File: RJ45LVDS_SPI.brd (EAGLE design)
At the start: 44.2 x 38 mm, 45 parts, among them J1 RJHSE-3381, U1 SN65MLVD206, U2 SN65MLVD206, U3 SN65MLVD206, U4 SN65MLVD206, U5 SN74LVC1T45DBVR, U6 SN74LVC1T45DBVR, U7 SN74LVC1T45DBVR, U8 SN74LVC1T45DBVR, U9 MIC39100-3.3WS

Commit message: tweaks
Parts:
- removed SJ13: (no value), jumper:SJ
- moved R5 6.60 mm to (36.5, 74.2)
- moved C14 0.23 mm to (14.5, 42.9)
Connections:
- removed net N$18: R5.2, SJ13.2
- net +3V3: now also R5.2; no longer SJ13.1
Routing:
- net N$18: track 4.46 -> 0.00 mm, vias 1 -> 0
- net N$19: track 4.63 -> 7.30 mm
- net N$15: track 41.1 -> 39.8 mm
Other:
- board text removed: "LED_EN"

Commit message: Bom added
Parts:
- added C11: .1u, rcl-dhs:C0603
- C10, C16, C9: device rcl-dhs:C1206K -> rcl:SMC_B
- moved R5 5.19 mm to (39.9, 70.3), turned to 90 degrees
- moved U9 0.74 mm to (44.4, 64.5)
- moved C16 0.56 mm to (46.5, 58.7)
- moved C10 0.35 mm to (43.6, 69.8)
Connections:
- net +3V3: now also C9.+; no longer C9.1
- net +5V: now also C10.+, C11.1; no longer C10.1
- net GND: now also C10.-, C11.2, C16.-, C9.-; no longer C10.2, C16.2, C9.2
- net N$16: now also C16.+; no longer C16.1
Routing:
- net N$19: track 7.30 -> 12.0 mm
- net N$17: track 3.72 -> 2.98 mm
- net +5V: track 6.54 -> 7.25 mm

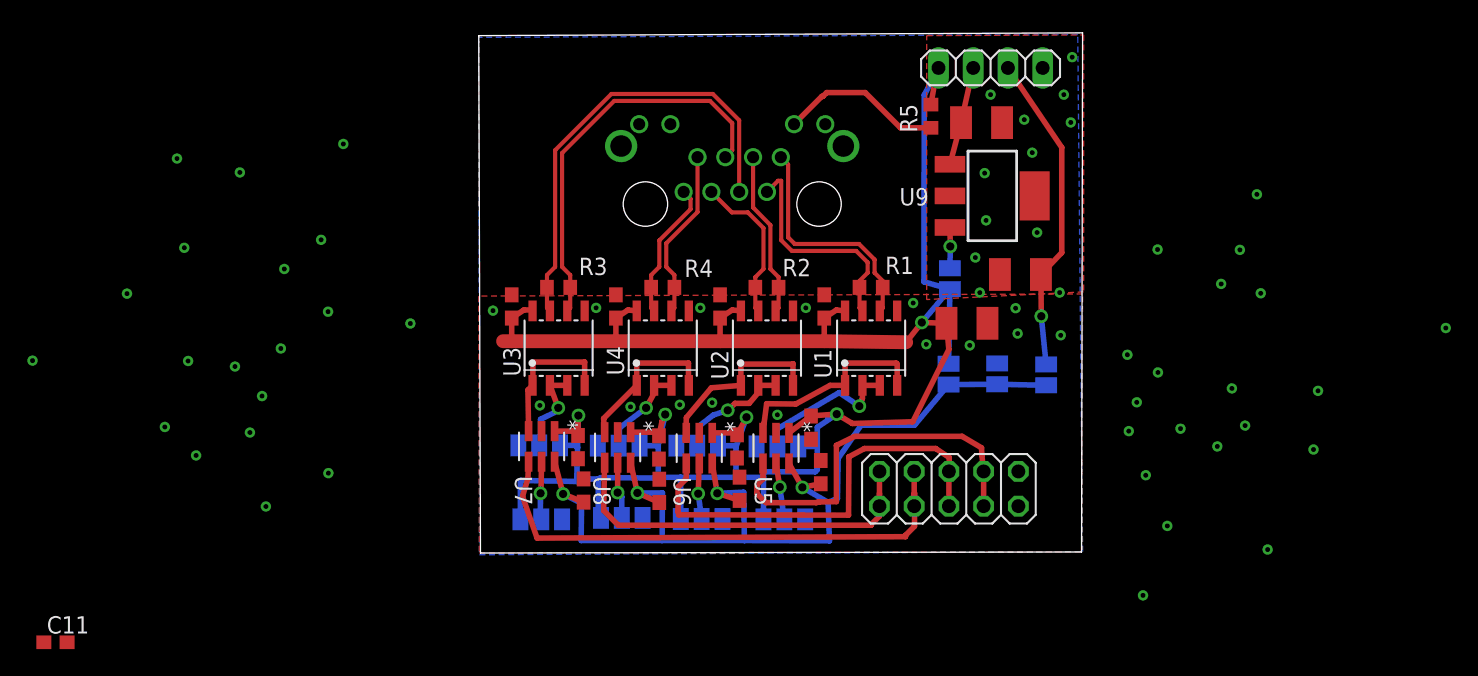
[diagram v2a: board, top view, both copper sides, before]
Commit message: Added mount holes
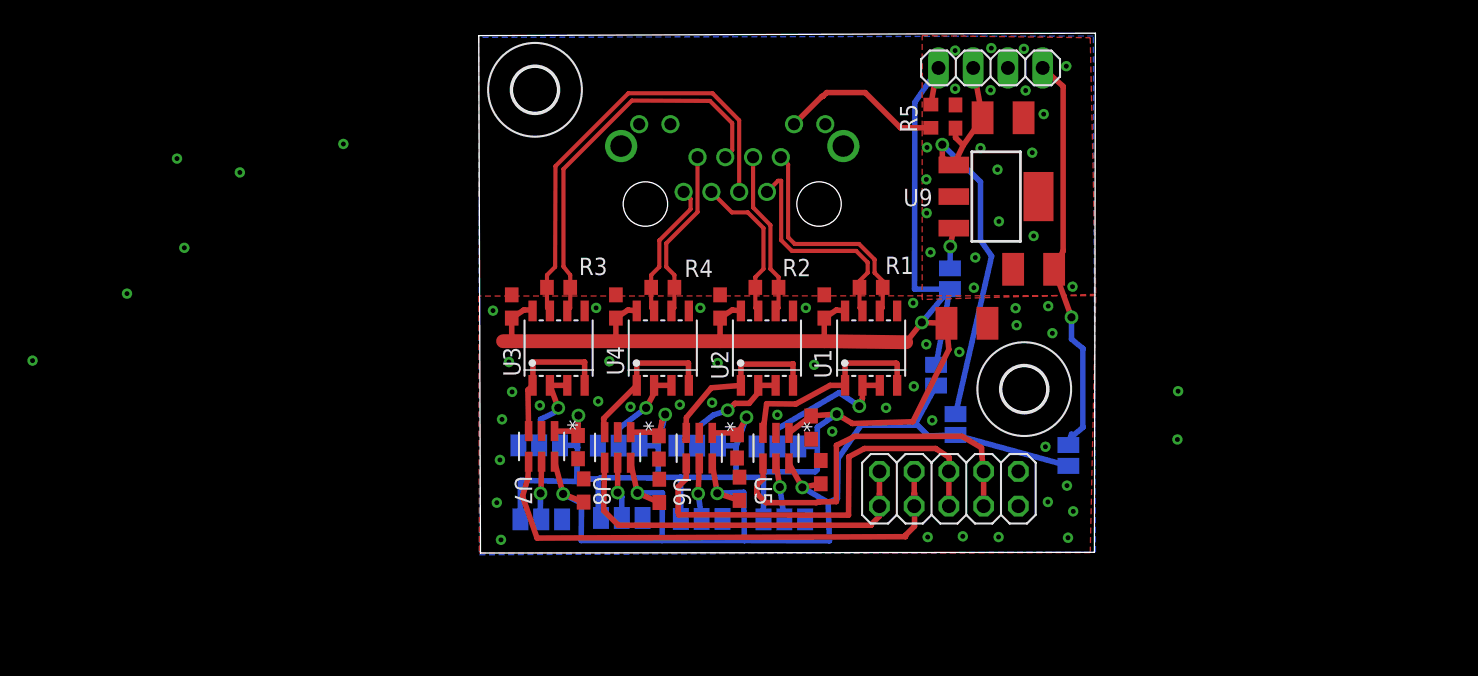
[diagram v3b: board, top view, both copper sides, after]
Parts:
- added U$1, U$2: (no value), holes:3,3
- moved C11 76.2 mm to (41.7, 70.3), turned to 90 degrees
- moved SJ11 6.11 mm to (50.0, 45.5)
- moved SJ10 4.80 mm to (41.7, 47.8)
- moved C10 1.61 mm to (45.2, 70.2)
- moved C16 1.04 mm to (47.4, 59.1)
- moved SJ9 0.92 mm to (40.3, 51.4)
- moved U9 0.28 mm to (44.7, 64.4)
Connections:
- net GND: now also JP2.3
- net N$16: now also JP2.4; no longer JP2.3
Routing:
- net +5V: track 7.25 -> 32.6 mm, vias 0 -> 1
- net N$16: track 23.5 -> 29.8 mm
- net N$12: track 75.1 -> 79.2 mm
- net +3V3: track 164.1 -> 165.7 mm
- net IN3_P: track 29.3 -> 28.4 mm
- net IN3_N: track 33.3 -> 32.6 mm
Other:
- board size 44.2 x 38 mm -> 45.1 x 38 mm

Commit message: layout tweaks
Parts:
- moved SJ10 18.6 mm to (47.4, 65.5), turned to 0 degrees
- moved SJ11 8.49 mm to (41.8, 47.7)
- moved C13 0.63 mm to (25.4, 43.4)
- moved U$2 0.51 mm to (47.0, 50.8)
- moved U$1 0.48 mm to (11.4, 72.4)
- moved C6 0.45 mm to (25.4, 46.5)
- moved C9 0.43 mm to (42.7, 55.6)
- moved C14 0.33 mm to (14.5, 42.6)
- moved C8 0.10 mm to (19.9, 46.1)
- moved C7 0.08 mm to (14.0, 46.1)
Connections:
- net N$12: no longer SJ10.1
- net N$16: now also SJ10.1
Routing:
- net N$16: track 29.8 -> 43.8 mm, vias 1 -> 0
- net +5V: track 32.6 -> 19.2 mm, vias 1 -> 0
- net N$12: track 79.2 -> 72.9 mm
- net N$14: track 32.0 -> 31.1 mm
- net N$8: track 28.6 -> 28.0 mm
- net +3V3: track 165.7 -> 166.2 mm
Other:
- board size 45.1 x 38 mm -> 45.1 x 38.5 mm

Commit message: Tidy up and update pdf
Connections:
- net N$12 renamed VCCIO
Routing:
- net +3V3: track 166.2 -> 131.9 mm
- net VCCIO: track 72.9 -> 63.5 mm
- net +5V: track 19.2 -> 9.92 mm
- net IN1_N: track 16.6 -> 15.5 mm
